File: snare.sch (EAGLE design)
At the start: 76 parts, among them IC1 TL072D, IC2 TL072D, T1 BC846, T2 BC856, T3 BC846, T4 2N3704, T5 BC846, T6 BC846, T7 BC846

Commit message: snare layout
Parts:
- added JP1: HEADER, Livestream:HEADER
- S3: value TRIGGER -> ACCENT
- renumbered U$1 to JP2
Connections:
- net +15V: now also JP1.2
- net -15V: now also JP1.1
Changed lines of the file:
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@@
 <attribute name="PARTNO" value="RMCF0805JT4K70"/>
 </part>
-<part name="S3" library="SparkFun-Electromechanical" deviceset="TAC_SWITCH" device="SMD" value="TRIGGER">
+<part name="S3" library="SparkFun-Electromechanical" deviceset="TAC_SWITCH" device="SMD" value="ACCENT">
 <attribute name="PARTNO" value="PTS525SM10SMTR LFS"/>
 </part>
@@
 <attribute name="PARTNO" value="RC2012J102CS"/>
 </part>
-<part name="U$1" library="Livestream" deviceset="AUDIO-JACK-3P" device="">
+<part name="JP2" library="Livestream" deviceset="AUDIO-JACK-3P" device="">
 <attribute name="PARTNO" value="SJ-3523-SMT-TR"/>
 </part>
@@
 <part name="C24" library="SparkFun-Capacitors" deviceset="CAP" device="0805" value="10nF"/>
 <part name="R39" library="SparkFun-Resistors" deviceset="RESISTOR" device="0805-RES" value="27k"/>
+<part name="JP1" library="Livestream" deviceset="HEADER" device=""/>
+<part name="SUPPLY34" library="supply2" deviceset="VCC" device="" value="+15v"/>
+<part name="SUPPLY35" library="supply2" deviceset="VCC" device="" value="-15V"/>
 </parts>
 <sheets>
@@
 <attribute name="PARTNO" x="190.5" y="48.26" size="1.778" layer="96" display="off"/>
 </instance>
-<instance part="U$1" gate="G$1" x="208.28" y="48.26" rot="R180">
+<instance part="JP2" gate="G$1" x="208.28" y="48.26" rot="R180">
 <attribute name="PARTNO" x="208.28" y="48.26" size="1.778" layer="96" display="off"/>
 </instance>
@@
 <instance part="C24" gate="G$1" x="134.62" y="-17.78" rot="R90"/>
 <instance part="R39" gate="G$1" x="147.32" y="7.62" rot="R90"/>
+<instance part="JP1" gate="G$1" x="38.1" y="142.24"/>
+<instance part="SUPPLY34" gate="G$1" x="48.26" y="149.86"/>
+<instance part="SUPPLY35" gate="G$1" x="48.26" y="137.16" rot="R180"/>
 </instances>
 <busses>
@@
 <wire x1="121.92" y1="10.16" x2="121.92" y2="5.08" width="0.1524" layer="91"/>
 </segment>
+<segment>
+<pinref part="JP1" gate="G$1" pin="2"/>
+<pinref part="SUPPLY34" gate="G$1" pin="VCC"/>
+<wire x1="45.72" y1="144.78" x2="48.26" y2="144.78" width="0.1524" layer="91"/>
+<wire x1="48.26" y1="144.78" x2="48.26" y2="147.32" width="0.1524" layer="91"/>
+</segment>
 </net>
 <net name="N$1" class="0">
@@
 </segment>
 <segment>
-<pinref part="U$1" gate="G$1" pin="SLEEVE"/>
+<pinref part="JP2" gate="G$1" pin="SLEEVE"/>
 <pinref part="SUPPLY12" gate="GND" pin="GND"/>
 <wire x1="203.2" y1="45.72" x2="200.66" y2="45.72" width="0.1524" layer="91"/>
@@
 <pinref part="SUPPLY33" gate="G$1" pin="VCC"/>
 <wire x1="121.92" y1="-30.48" x2="121.92" y2="-33.02" width="0.1524" layer="91"/>
+</segment>
+<segment>
+<pinref part="JP1" gate="G$1" pin="1"/>
+<pinref part="SUPPLY35" gate="G$1" pin="VCC"/>
+<wire x1="45.72" y1="142.24" x2="48.26" y2="142.24" width="0.1524" layer="91"/>
+<wire x1="48.26" y1="142.24" x2="48.26" y2="139.7" width="0.1524" layer="91"/>
 </segment>
 </net>
@@
 <segment>
 <pinref part="R20" gate="G$1" pin="2"/>
-<pinref part="U$1" gate="G$1" pin="RIGHT"/>
+<pinref part="JP2" gate="G$1" pin="RIGHT"/>
 <wire x1="195.58" y1="48.26" x2="200.66" y2="48.26" width="0.1524" layer="91"/>
-<pinref part="U$1" gate="G$1" pin="LEFT"/>
+<pinref part="JP2" gate="G$1" pin="LEFT"/>
 <wire x1="200.66" y1="48.26" x2="203.2" y2="48.26" width="0.1524" layer="91"/>
 <wire x1="203.2" y1="50.8" x2="200.66" y2="50.8" width="0.1524" layer="91"/>

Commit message: added bom for snare
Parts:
- C1, C5, C6: PARTNO (none) -> C0805C682K5RACTU
- C19: PARTNO (none) -> C0805C102K5RACTU
- C2, C3: PARTNO (none) -> CC0805KRX7R9BB273
- C20: PARTNO (none) -> CC0805KRX7R9BB272
- C21: PARTNO (none) -> CL21B223KBANNNC
- C22, C23: PARTNO (none) -> 08055C182KAT2A
- C24: PARTNO (none) -> GRM216R71H103KA01D
- C4, C7: PARTNO (none) -> C0805C473K5RACTU
- C8: PARTNO (none) -> CC0805KRX7R9BB221
- C9: PARTNO (none) -> EEE-1AA330WAR
- R1, R36, R38: PARTNO RMCF0805JT22K0 -> RMCF0805FT22K0
- R10: PARTNO (none) -> RMCF0805FT220R
- R11, R21, R25: PARTNO RC2012F105CS -> RMCF0805FT1M00
- R12: PARTNO (none) -> RMCF0805FT2K20
- R13, R18, R37: PARTNO RMCF0805JT47K0 -> RMCF0805FT47K0
- R14: PARTNO (none) -> 296UD104B1N
- R15: PARTNO (none) -> PTV09A-4025F-A203
- R16: PARTNO (none) -> PTV09A-2020F-A104
- R17, R5: PARTNO RC2012J104CS -> RMCF0805FT100K
- R19: PARTNO RMCF0805JT470K -> CRCW0805470KFKEA
- R2, R3: PARTNO RC2012J103CS -> RMCF0805FT10K0
- R20, R28: PARTNO RC2012J102CS -> RMCF0805FT1K00
- R22: PARTNO (none) -> RMCF0805FT330K
- R23: PARTNO (none) -> RMCF0805FT300K
- R24, R4: PARTNO RMCF0805JT4K70 -> RMCF0805FT4K70
- R26, R31, R34: PARTNO (none) -> RMCF0805FT100R
- R27: PARTNO (none) -> PTV09A-4020F-A103
- R29: PARTNO (none) -> RMCF0805FT33K0
- R30: PARTNO (none) -> RMCF0805FT330R
- R32, R33: PARTNO (none) -> RMCF0805FT15K0
- R35: PARTNO (none) -> RC0805FR-072M2L
- R39: PARTNO (none) -> RMCF0805FT27K0
- R6, R7: PARTNO (none) -> RMCF0805FT680R
- R8: PARTNO (none) -> RMCF0805FT820R
- R9: PARTNO RMCF0805JT8K20 -> RMCF0805FT8K20

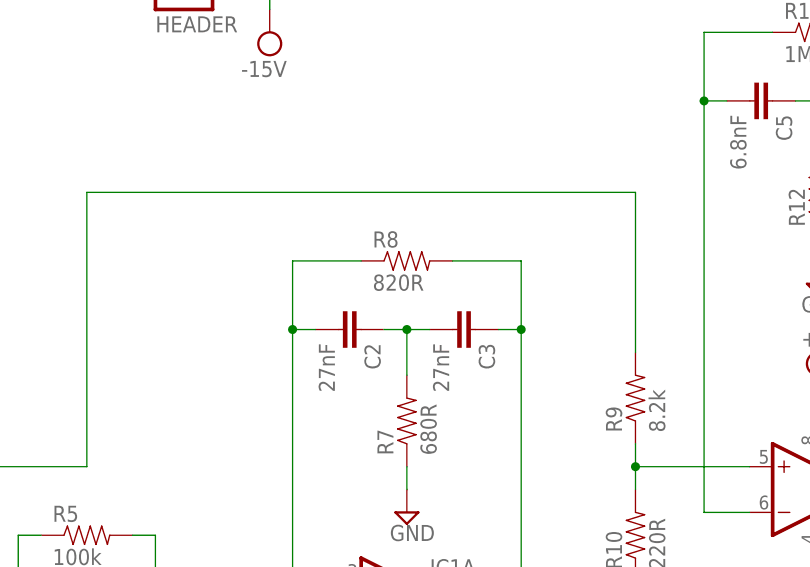
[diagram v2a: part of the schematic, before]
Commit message: fixed some part numbers
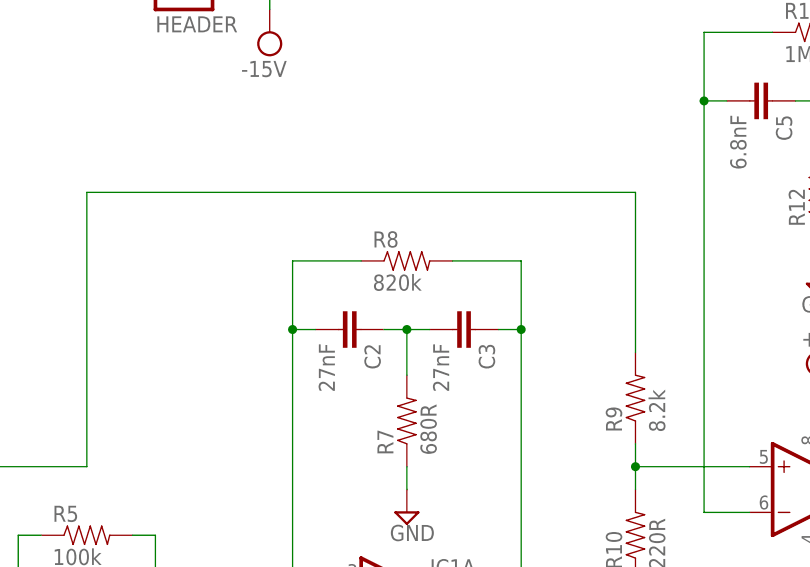
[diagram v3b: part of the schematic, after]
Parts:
- R8: value 820R -> 820k; PARTNO RMCF0805FT820R -> RC0805FR-07820KL
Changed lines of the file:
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@@
 </part>
 <part name="SUPPLY6" library="supply2" deviceset="GND" device=""/>
-<part name="R8" library="SparkFun-Resistors" deviceset="RESISTOR" device="0805-RES" value="820R">
-<attribute name="PARTNO" value="RMCF0805FT820R"/>
+<part name="R8" library="SparkFun-Resistors" deviceset="RESISTOR" device="0805-RES" value="820k">
+<attribute name="PARTNO" value="RC0805FR-07820KL"/>
 </part>
 <part name="C4" library="SparkFun-Capacitors" deviceset="CAP" device="0805" value="47nF">
